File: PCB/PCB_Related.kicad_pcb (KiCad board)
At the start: 4 copper layers, 98.4 x 41.3 mm, 16 parts, among them SW1 RotaryEncoder_Switch, U4 MOUDLE-SEEEDUINO-XIAO

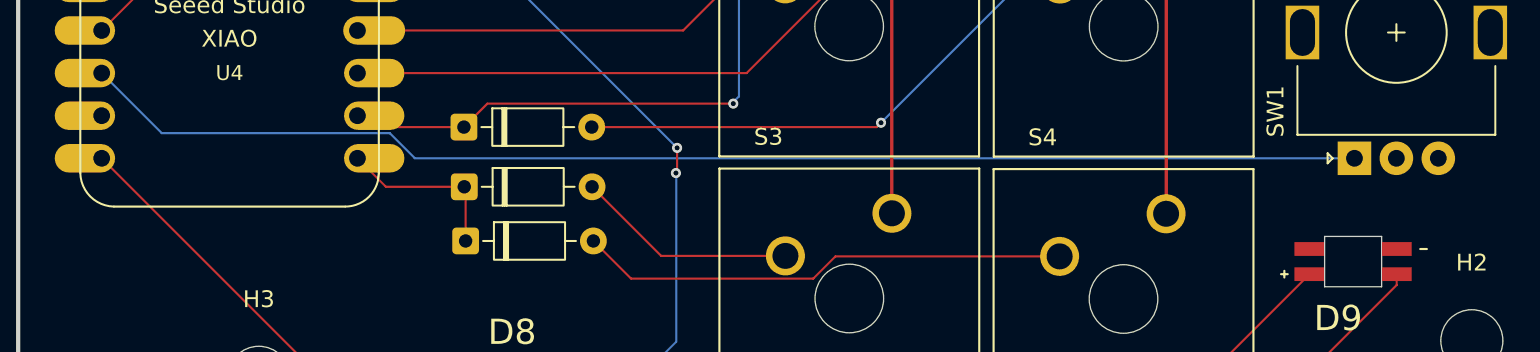
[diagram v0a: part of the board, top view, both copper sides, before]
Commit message: Fixed Footprint and updated picture
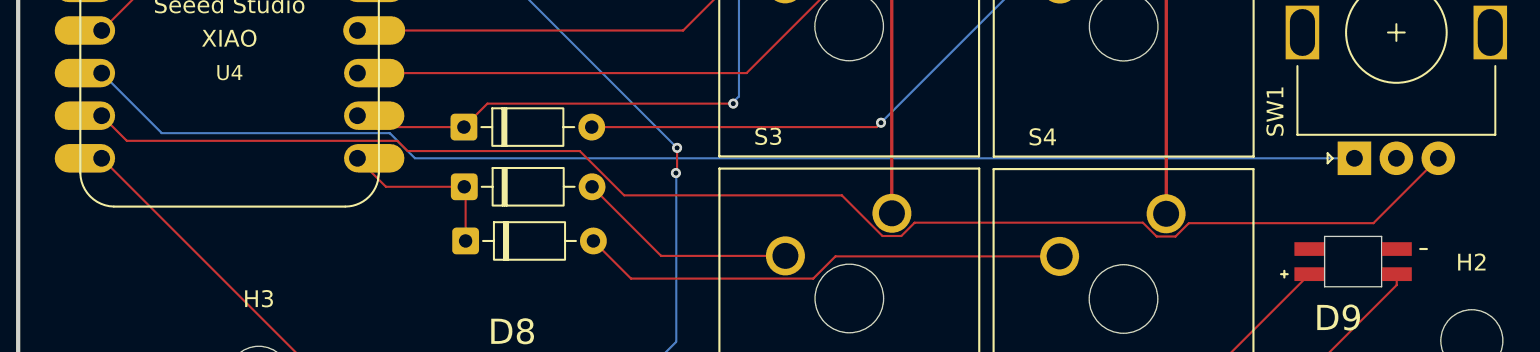
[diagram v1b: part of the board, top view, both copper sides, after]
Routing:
- net BDOWN: track 0.00 -> 85.3 mm
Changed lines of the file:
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@@
+	)
+	(segment
+		(start 113.24355 52.430659)
+		(end 112.450659 53.22355)
+		(width 0.127)
+		(layer "F.Cu")
+		(net 12)
+	)
+	(segment
+		(start 140.599341 52.460659)
+		(end 129.59355 52.460659)
+		(width 0.127)
+		(layer "F.Cu")
+		(net 12)
+	)
+	(segment
+		(start 111.329341 53.22355)
+		(end 108.905791 50.8)
+		(width 0.127)
+		(layer "F.Cu")
+		(net 12)
+	)
+	(segment
+		(start 126.85645 52.430659)
+		(end 113.24355 52.430659)
+		(width 0.127)
+		(layer "F.Cu")
+		(net 12)
+	)
+	(segment
+		(start 83.0115 48.158597)
+		(end 82.401403 47.5485)
+		(width 0.127)
+		(layer "F.Cu")
+		(net 12)
+	)
+	(segment
+		(start 127.679341 53.25355)
+		(end 126.85645 52.430659)
+		(width 0.127)
+		(layer "F.Cu")
+		(net 12)
+	)
+	(segment
+		(start 95.922193 50.8)
+		(end 93.28079 48.158597)
+		(width 0.127)
+		(layer "F.Cu")
+		(net 12)
+	)
+	(segment
+		(start 129.59355 52.460659)
+		(end 128.800659 53.25355)
+		(width 0.127)
+		(layer "F.Cu")
+		(net 12)
+	)
+	(segment
+		(start 112.450659 53.22355)
+		(end 111.329341 53.22355)
+		(width 0.127)
+		(layer "F.Cu")
+		(net 12)
+	)
+	(segment
+		(start 93.28079 48.158597)
+		(end 83.0115 48.158597)
+		(width 0.127)
+		(layer "F.Cu")
+		(net 12)
+	)
+	(segment
+		(start 128.800659 53.25355)
+		(end 127.679341 53.25355)
+		(width 0.127)
+		(layer "F.Cu")
+		(net 12)
+	)
+	(segment
+		(start 144.47 48.59)
+		(end 140.599341 52.460659)
+		(width 0.127)
+		(layer "F.Cu")
+		(net 12)
+	)
+	(segment
+		(start 66.2685 47.5485)
+		(end 64.77 46.05)
+		(width 0.127)
+		(layer "F.Cu")
+		(net 12)
+	)
+	(segment
+		(start 108.905791 50.8)
+		(end 95.922193 50.8)
+		(width 0.127)
+		(layer "F.Cu")
+		(net 12)
+	)
+	(segment
+		(start 82.401403 47.5485)
+		(end 66.2685 47.5485)
+		(width 0.127)
+		(layer "F.Cu")
+		(net 12)
 	)
 	(segment
